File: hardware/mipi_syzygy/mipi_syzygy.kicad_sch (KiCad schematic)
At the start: 2 parts

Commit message: Working on mipi board
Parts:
- removed J?: Conn_01x15_MountingPin, symbol Connector_Generic_MountingPin:Conn_01x15_MountingPin
- added H1, H2: MountingHole_Pad, SYZYGY:MountingHole_3.2mm_M3_6.5mm_Pad_TopBottom, symbol Mechanical:MountingHole_Pad
- added J1: Conn_01x15, Connector_FFC-FPC:Hirose_FH12-15S-0.5SH_1x15-1MP_P0.50mm_Horizontal, symbol Connector_Generic:Conn_01x15
- gave numbers to parts that had none: 1
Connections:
- net +3.3V: now also J1.15 (Pin_15)
- net CAM_CK_N: now also J1.8 (Pin_8)
- net CAM_CK_P: now also J1.9 (Pin_9)
- net CAM_D0_N: now also J2.8 (S3_D1N), J1.2 (Pin_2); no longer J2.7 (S2_D0N)
- net CAM_D0_P: now also J2.6 (S1_D1P), J1.3 (Pin_3); no longer J2.5 (S0_D0P)
- net CAM_D1_N: now also J2.12 (S7_D3N), J1.5 (Pin_5); no longer J2.8 (S3_D1N)
- net CAM_D1_P: now also J2.10 (S5_D3P), J1.6 (Pin_6); no longer J2.6 (S1_D1P)
- net CAM_IO0: now also J2.21 (S16), J1.11 (Pin_11); no longer J2.31 (S26)
- net CAM_IO1: now also J2.23 (S18), J1.12 (Pin_12); no longer J2.32 (S27)
- net CAM_SCL: now also J2.25 (S20), J1.13 (Pin_13); no longer J2.30 (S25)
- net CAM_SDA: now also J2.27 (S22), J1.14 (Pin_14); no longer J2.29 (S24)
- net GND: now also J1.1 (Pin_1), J1.10 (Pin_10), J1.4 (Pin_4), J1.7 (Pin_7)
- no-connect marks 0 -> 30
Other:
- note added: "Back"
- note added: "Front"
- note added: "Mounting Holes"
- moved on the sheet: J2

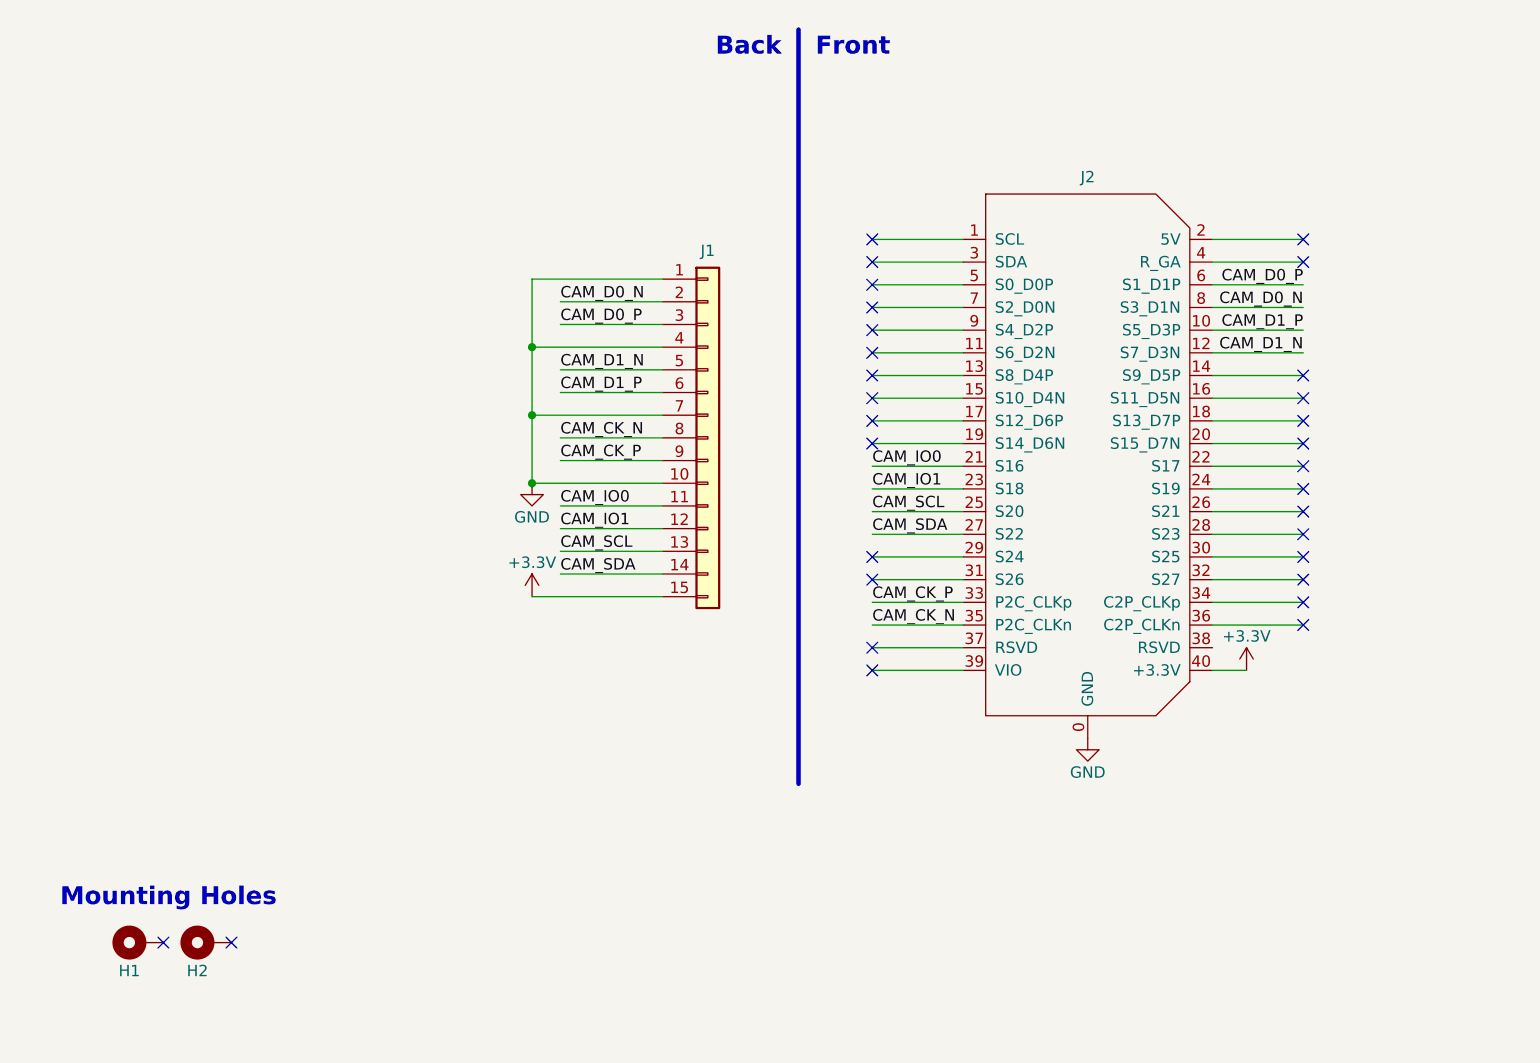
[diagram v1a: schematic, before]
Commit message: Routed mipi board
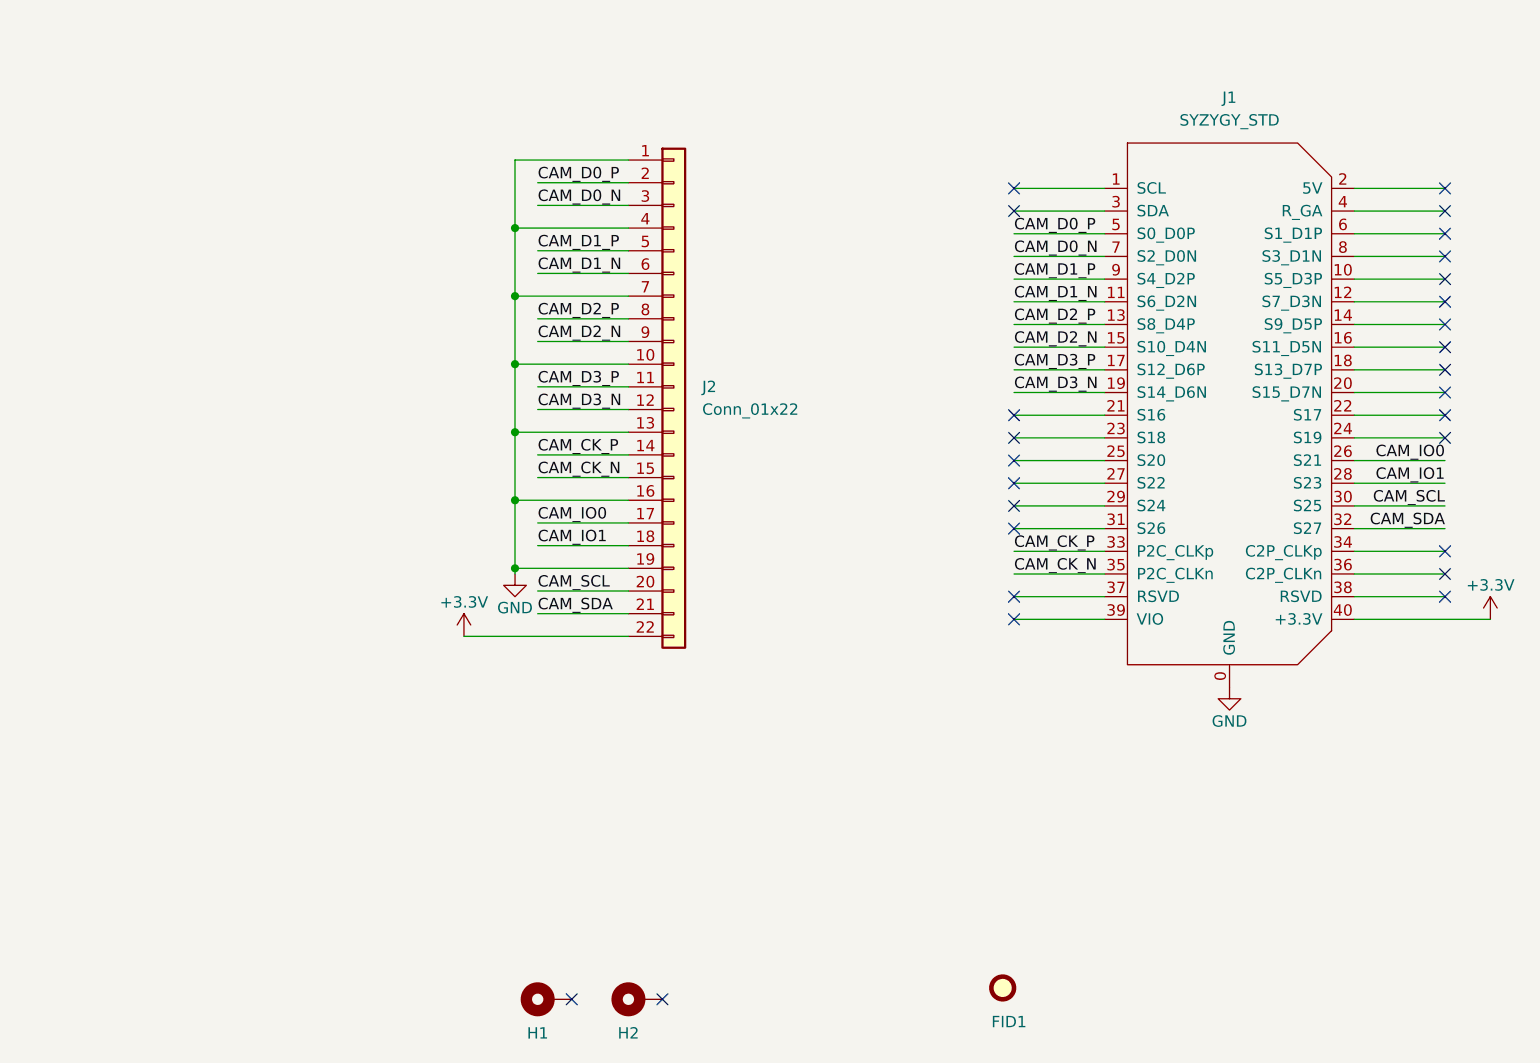
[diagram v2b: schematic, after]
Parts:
- removed J1: Conn_01x15, Connector_FFC-FPC:Hirose_FH12-15S-0.5SH_1x15-1MP_P0.50mm_Horizontal, symbol Connector_Generic:Conn_01x15
- removed J2: SYZYGY_STD, SYZYGY:QTE-020-01-F-D-A, symbol SYZYGY:SYZYGY_STD
- added FID1: Fiducial, Fiducial:Fiducial_1mm_Mask2mm, symbol Mechanical:Fiducial
- added J1: SYZYGY_STD, SYZYGY:QTE-020-01-F-D-A, symbol SYZYGY:SYZYGY_STD
- added J2: Conn_01x22, Connector_FFC-FPC:Hirose_FH12-22S-0.5SH_1x22-1MP_P0.50mm_Horizontal, symbol Connector_Generic:Conn_01x22
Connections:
- net +3.3V: now also J1.40 (+3.3V), J2.22 (Pin_22)
- net CAM_CK_N: now also J1.35 (P2C_CLKn), J2.15 (Pin_15)
- net CAM_CK_P: now also J1.33 (P2C_CLKp), J2.14 (Pin_14)
- net CAM_D0_N: now also J1.7 (S2_D0N), J2.3 (Pin_3)
- net CAM_D0_P: now also J1.5 (S0_D0P), J2.2 (Pin_2)
- net CAM_D1_N: now also J1.11 (S6_D2N), J2.6 (Pin_6)
- net CAM_D1_P: now also J1.9 (S4_D2P), J2.5 (Pin_5)
- net CAM_IO0: now also J1.26 (S21), J2.17 (Pin_17)
- net CAM_IO1: now also J1.28 (S23), J2.18 (Pin_18)
- net CAM_SCL: now also J1.30 (S25), J2.20 (Pin_20)
- net CAM_SDA: now also J1.32 (S27), J2.21 (Pin_21)
- net GND: now also J1.0 (GND), J2.1 (Pin_1), J2.10 (Pin_10), J2.13 (Pin_13), J2.16 (Pin_16), J2.19 (Pin_19), J2.4 (Pin_4), J2.7 (Pin_7)
- new net CAM_D2_N: J1.15 (S10_D4N), J2.9 (Pin_9)
- new net CAM_D2_P: J1.13 (S8_D4P), J2.8 (Pin_8)
- new net CAM_D3_N: J1.19 (S14_D6N), J2.12 (Pin_12)
- new net CAM_D3_P: J1.17 (S12_D6P), J2.11 (Pin_11)
- no-connect marks 30 -> 27
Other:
- note removed: "Back"
- note removed: "Front"
- note removed: "Mounting Holes"
